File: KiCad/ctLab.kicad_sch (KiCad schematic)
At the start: 58 parts, among them U1 7815, U10 XPort-01, U2 7915, U3 7805, U4 7805, U5 FT232RL, U6 6N137, U8 LF33, U9 MAX232

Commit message: starting IFP schematics
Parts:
- removed PL1: Pfosten 14-pol., symbol Connector_Generic:Conn_02x07_Odd_Even
- removed TR1: Flachtrafo 2 x 15 V, 6 VA (Block), symbol Device:Transformer_1P_2S
- removed TR2: Flachtrafo 2 x 9 V, 6 VA (Block), symbol Device:Transformer_1P_2S
- added PL1: (no value), symbol Connector:Conn_01x14_Socket
- added TR1: (no value), symbol Transformer:TRANSF6
- added TR2: Flachtrafo 2 x 9 V, 6 VA (Block), symbol Transformer:TRANSF6
- PL2: value Pfosten 10-pol. -> OPTO-BUS
- PL3: value Schraubklemme RM 7,5 -> 230V AC
- PL4: value USB-B Printbuchse -> (none)
- R1: value 0R (nur zum Test bestücken) -> 0R
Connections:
- net at PL3.1 (Pin_1): now also TR1.1, TR2.1
- net at PL3.2 (Pin_2): now also TR1.4, TR2.4
- net GND: now reaches U9.15 (GND)
- net GND: now also C12.2, C14.2, C23.2, C3.2, C7.2, PL4.4 (GND), PL4.SH (Shield), R8.2, RB3.3 (-), U3.2 (GND), U5.18 (GND), U5.21 (GND), U5.25 (AGND), U5.7 (GND), U6.5 (GND)
- net VCC: now reaches U9.16 (VCC)
- net VCC: now also C7.1, D2.1 (K), U3.3 (OUT), U5.20 (VCC), U5.4 (VCCIO), U6.8 (VCC)
- net -15V | 1: now reaches C5.1
- net -15V | 1: now also U2.3 (VO), PL1.10 (Pin_10), PL1.9 (Pin_9)
- net GND | 1: now reaches C5.2
- net GND | 1: now also C1.2, C10.2, C4.2, C8.2, C9.1, R1.1, U1.2 (GND), U2.1 (GND), PL1.7 (Pin_7), PL1.8 (Pin_8), TR1.6, TR1.7
- net 9V | 3: now reaches U4.1 (IN)
- net 9V | 3: now also C11.1, C2.1, RB2.1 (+), PL1.1 (Pin_1), PL1.2 (Pin_2)
- net GND | 2: now reaches U4.2 (GND)
- net GND | 2: now also C11.2, C2.2, C6.2, R1.2, RB2.3 (-), PL1.11 (Pin_11), PL1.12 (Pin_12), PL1.3 (Pin_3), PL1.4 (Pin_4)
- net 9V | 2: now reaches U4.3 (OUT)
- net 9V | 2: now also C6.1, PL1.13 (Pin_13), PL1.14 (Pin_14)
- net at RB3.1 (+): now also C12.1, C3.1, U3.1 (IN)
- net at JP1.1 (A): now also U5.1 (TXD)
- net at JP1.2 (B): now also D3.1 (K)
- net at C8.1: now also C9.2, RB1.3 (-), U2.2 (VI)
- net at U5.15 (USBD+): now also PL4.3 (D+)
- net at U5.16 (USBD-): now also PL4.2 (D-)
- net at U5.19 (~{RESET}): now also R7.2, R8.1
- net at U5.26 (TEST): now also C23.1
- net at U5.5 (RXD): now also U6.6 (VO)
- net at JP2.2 (B): now also D4.1 (K)
- net at D4.2 (A): now also D1.2 (A), D3.2 (A), R3.2, R5.2
- net at R3.1: now also PL2.1 (Pin_1), PL2.2 (Pin_2)
- net at R4.1: now also U6.2 (A)
- net at R4.2: now also PL2.10 (Pin_10), PL2.9 (Pin_9)
- net at PL4.1 (VBUS): now also C14.1, L1.1
- net at U6.3 (C): now also PL2.7 (Pin_7), PL2.8 (Pin_8)
- net at U6.7 (EN): now also PL2.3 (Pin_3), PL2.4 (Pin_4)
- net at C10.1: now also C1.1, RB1.1 (+), U1.1 (IN)
- net at R7.1: now also D2.2 (A), L1.2
- net at RB2.2: now also TR2.7
- net at RB2.4: now also TR2.8
- net +15V | 1: now reaches C4.1
- net +15V | 1: now also U1.3 (OUT), PL1.5 (Pin_5), PL1.6 (Pin_6)
- net at D1.1 (K): now also JP3.2 (B)
- net at RB1.2: now also TR1.5
- net at RB1.4: now also TR1.8
- new net: TR2.2, TR2.3
- new net: TR1.2, TR1.3
- no-connect marks 0 -> 15
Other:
- moved on the sheet: C1, C10, C11, C12, C18, C19, C2, C20, C21, C22, C24, C3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

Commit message: cont. working on IFP
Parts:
- removed C1, C14, C19, C2, C22, C23, C24, C3, C4, C5, C6, C7, C8: 100n ker. RMS, symbol Device:C
- removed C10, C11, C12, C9: 470µ 35V, symbol Device:C_Polarized
- removed C13, C15: 47µ 6V3, symbol Device:C_Polarized
- removed C16, C17, C18, C21: 11µ 50V, symbol Device:C_Polarized
- removed C20: 4µ7 35V, symbol Device:C_Polarized
- removed D1, D3, D4: 1N4148, symbol Diode:1N4148
- removed D2: 1N4004, symbol Diode:1N4004
- removed JP1, JP2, JP3: Jumper, symbol Jumper:Jumper_2_Open
- removed L1: 10µH axial, symbol Device:L
- removed PL1: (no value), symbol Connector:Conn_01x14_Socket
- removed PL2: OPTO-BUS, symbol Connector_Generic:Conn_02x05_Odd_Even
- removed PL3: 230V AC, symbol Connector:Screw_Terminal_01x02
- removed PL4: (no value), symbol Connector:USB_B
- removed R1: 0R, symbol Device:R
- removed R2, R3: 220R, symbol Device:R
- removed R4: 2k7, symbol Device:R
- removed R5: 2k2, symbol Device:R
- removed R7: 4k7, symbol Device:R
- removed R8: 10k, symbol Device:R
- removed RB1, RB2, RB3: B80C1500, symbol Diode_Bridge:B80C1500G
- removed RS1: D-Sub 9-pol. F, symbol Connector:DE9_Socket
- removed TR1: (no value), symbol Transformer:TRANSF6
- removed TR2: Flachtrafo 2 x 9 V, 6 VA (Block), symbol Transformer:TRANSF6
- removed U1: 7815, symbol Regulator_Linear:L7815
- removed U10: XPort-01, symbol Connector_Generic:Conn_02x12_Odd_Even
- removed U2: 7915, symbol Regulator_Linear:L7915
- removed U3, U4: 7805, symbol Regulator_Linear:L7805
- removed U5: FT232RL, symbol Interface_USB:FT232RL
- removed U6: 6N137, symbol Isolator:6N137
- removed U8: LF33, symbol Regulator_Linear:LF33_TO220
- removed U9: MAX232, symbol Interface_UART:MAX232
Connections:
- no-connect marks 15 -> 0
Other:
- added sheet IFP (Interface and Power Supply) (ifp.kicad_sch)

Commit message: finishing IFP and starting DCG drawing
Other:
- added sheet DCG (Direct Current Generator) (dcg.kicad_sch)
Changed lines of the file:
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@@
 	(paper "A3")
+	(sheet
+		(at 116.84 30.48)
+		(size 45.72 44.45)
+		(exclude_from_sim no)
+		(in_bom yes)
+		(on_board yes)
+		(dnp no)
+		(fields_autoplaced yes)
+		(stroke
+			(width 0.1524)
+			(type solid)
+		)
+		(fill
+			(color 0 0 0 0)
+		)
+		(property "Sheetname" "DCG (Direct Current Generator)"
+			(at 116.84 29.7684 0)
+			(show_name no)
+			(do_not_autoplace no)
+			(effects
+				(font
+					(size 1.27 1.27)
+				)
+				(justify left bottom)
+			)
+		)
+		(property "Sheetfile" "dcg.kicad_sch"
+			(at 116.84 75.5146 0)
+			(show_name no)
+			(do_not_autoplace no)
+			(effects
+				(font
+					(size 1.27 1.27)
+				)
+				(justify left top)
+			)
+		)
+		(instances
+			(project "ctLab"
+				(path "/207e0f0e-27e8-440d-b34e-edbac4dab547"
+					(page "3")
+				)
+			)
+		)
+	)
 	(sheet
 		(at 30.48 31.75)

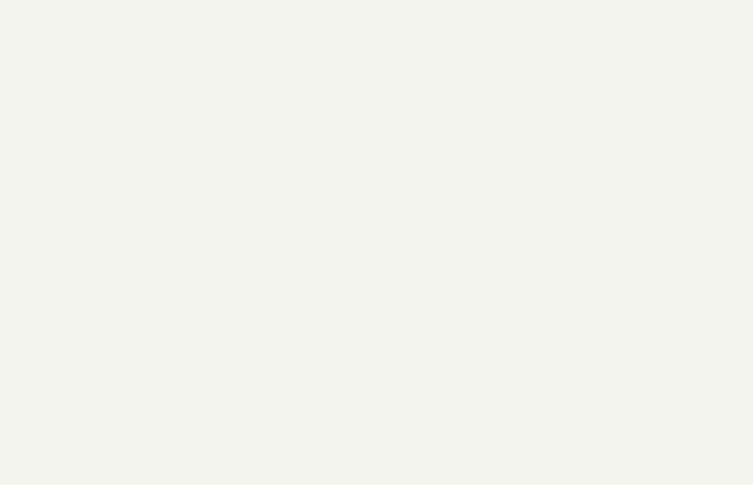
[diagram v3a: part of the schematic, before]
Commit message: drawing ADA/IO schematics
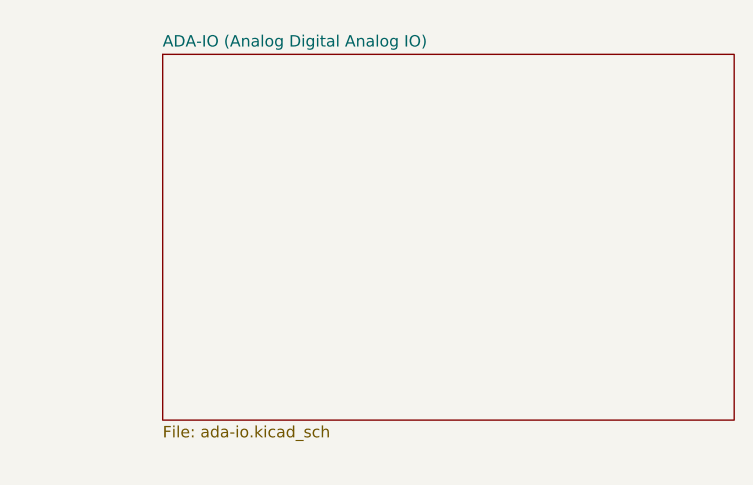
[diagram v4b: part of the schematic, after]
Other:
- added sheet ADA-IO (Analog Digital Analog IO) (ada-io.kicad_sch)
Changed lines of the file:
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@@
+	)
+	(sheet
+		(at 187.96 31.75)
+		(size 63.5 40.64)
+		(exclude_from_sim no)
+		(in_bom yes)
+		(on_board yes)
+		(dnp no)
+		(fields_autoplaced yes)
+		(stroke
+			(width 0.1524)
+			(type solid)
+		)
+		(fill
+			(color 0 0 0 0)
+		)
+		(property "Sheetname" "ADA-IO (Analog Digital Analog IO)"
+			(at 187.96 31.0384 0)
+			(show_name no)
+			(do_not_autoplace no)
+			(effects
+				(font
+					(size 1.27 1.27)
+				)
+				(justify left bottom)
+			)
+		)
+		(property "Sheetfile" "ada-io.kicad_sch"
+			(at 187.96 72.9746 0)
+			(show_name no)
+			(do_not_autoplace no)
+			(effects
+				(font
+					(size 1.27 1.27)
+				)
+				(justify left top)
+			)
+		)
+		(instances
+			(project "ctLab"
+				(path "/207e0f0e-27e8-440d-b34e-edbac4dab547"
+					(page "4")
+				)
+			)
+		)
 	)
 	(sheet
